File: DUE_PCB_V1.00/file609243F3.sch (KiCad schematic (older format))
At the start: 20 parts, among them J26 Motor Left, J27 Cutter Motor, J28 Motor Right, U1 MC33926, U2 MC33926

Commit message: Remove 2x4 Motor Pin Connectors
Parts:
- removed J26: Motor Left, Connector_PinSocket_2.54mm:PinSocket_2x04_P2.54mm_Vertical, symbol Connector_Generic:Conn_02x04_Top_Bottom
- removed J27: Cutter Motor, Connector_PinSocket_2.54mm:PinSocket_2x04_P2.54mm_Vertical, symbol Connector_Generic:Conn_02x04_Top_Bottom
- removed J28: Motor Right, Connector_PinSocket_2.54mm:PinSocket_2x04_P2.54mm_Vertical, symbol Connector_Generic:Conn_02x04_Top_Bottom
- removed JP4, JP5, JP6: 5V, Connector_PinSocket_2.54mm:PinSocket_1x02_P2.54mm_Vertical, symbol Jumper:Jumper_2_Open
- removed R17, R19, R21, R23, R25, R27: 1.5KO, Resistor_THT:R_Axial_DIN0207_L6.3mm_D2.5mm_P2.54mm_Vertical, symbol Device:R
- removed R18, R20, R22, R24, R26, R28: 1KO, Resistor_THT:R_Axial_DIN0207_L6.3mm_D2.5mm_P2.54mm_Vertical, symbol Device:R
- added D5: 1N5819, Diode_THT:D_DO-41_SOD81_P10.16mm_Horizontal, symbol Diode:1N5819
- added J32: 24V In, TerminalBlock:TerminalBlock_bornier-2_P5.08mm, symbol Connector:Screw_Terminal_01x02
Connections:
- net +24V: now also D5.1 (K)
- net GND: now also J32.1 (Pin_1)
- new net: D5.2 (A), J32.2 (Pin_2)
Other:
- moved on the sheet: U1, U2

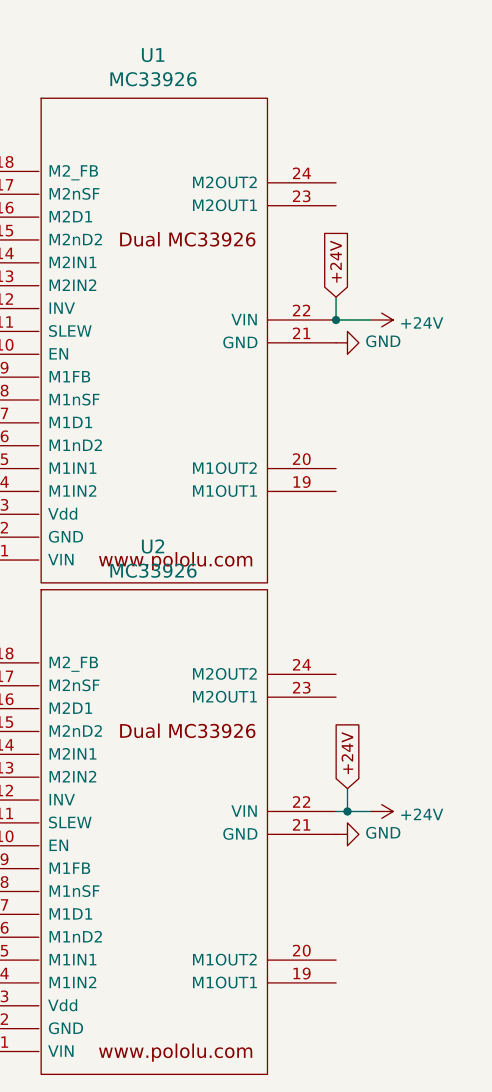
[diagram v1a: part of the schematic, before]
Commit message: Add Connector 24V for Motor & Cutter
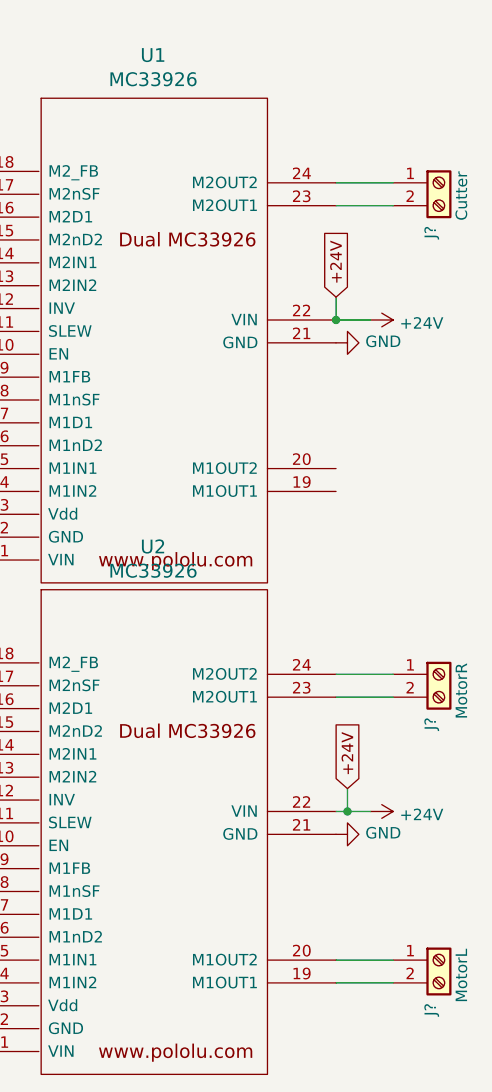
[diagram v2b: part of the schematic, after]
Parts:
- added J?: Cutter, TerminalBlock:TerminalBlock_bornier-2_P5.08mm, symbol Connector:Screw_Terminal_01x02
- added J?: MotorR, TerminalBlock:TerminalBlock_bornier-2_P5.08mm, symbol Connector:Screw_Terminal_01x02
- added J?: MotorL, TerminalBlock:TerminalBlock_bornier-2_P5.08mm, symbol Connector:Screw_Terminal_01x02
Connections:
- net at U2.19 (M1OUT1): now also J?.2 (Pin_2)
- net at U2.20 (M1OUT2): now also J?.1 (Pin_1)
- net at U2.23 (M2OUT1): now also J?.2 (Pin_2)
- net at U2.24 (M2OUT2): now also J?.1 (Pin_1)
- net at U1.23 (M2OUT1): now also J?.2 (Pin_2)
- net at U1.24 (M2OUT2): now also J?.1 (Pin_1)
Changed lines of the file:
@@
 Wire Wire Line
 	1350 950  1500 950
+$Comp
+L Connector:Screw_Terminal_01x02 J?
+U 1 1 60E7534A
+P 6350 1350
+F 0 "J?" V 6314 1162 50  0000 R CNN
+F 1 "Cutter" V 6450 1400 50  0000 R CNN
+F 2 "TerminalBlock:TerminalBlock_bornier-2_P5.08mm" H 6350 1350 50  0001 C CNN
+F 3 "~" H 6350 1350 50  0001 C CNN
+	1    6350 1350
+	1    0    0    -1
+$EndComp
+Wire Wire Line
+	5900 1350 6150 1350
+Wire Wire Line
+	5900 1450 6150 1450
+$Comp
+L Connector:Screw_Terminal_01x02 J?
+U 1 1 60E78788
+P 6350 3500
+F 0 "J?" V 6314 3312 50  0000 R CNN
+F 1 "MotorR" V 6450 3550 50  0000 R CNN
+F 2 "TerminalBlock:TerminalBlock_bornier-2_P5.08mm" H 6350 3500 50  0001 C CNN
+F 3 "~" H 6350 3500 50  0001 C CNN
+	1    6350 3500
+	1    0    0    -1
+$EndComp
+Wire Wire Line
+	5900 3500 6150 3500
+Wire Wire Line
+	5900 3600 6150 3600
+$Comp
+L Connector:Screw_Terminal_01x02 J?
+U 1 1 60E799F8
+P 6350 4750
+F 0 "J?" V 6314 4562 50  0000 R CNN
+F 1 "MotorL" V 6450 4800 50  0000 R CNN
+F 2 "TerminalBlock:TerminalBlock_bornier-2_P5.08mm" H 6350 4750 50  0001 C CNN
+F 3 "~" H 6350 4750 50  0001 C CNN
+	1    6350 4750
+	1    0    0    -1
+$EndComp
+Wire Wire Line
+	5900 4750 6150 4750
+Wire Wire Line
+	5900 4850 6150 4850
 $EndSCHEMATC

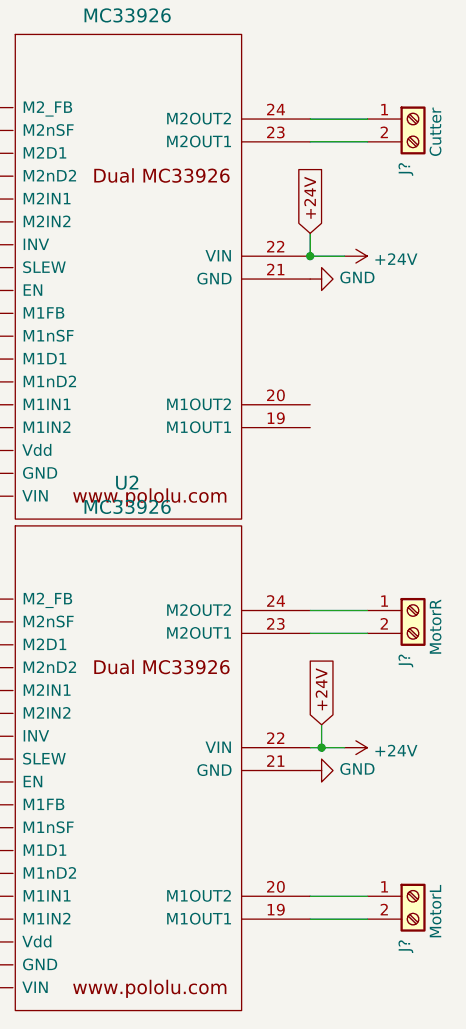
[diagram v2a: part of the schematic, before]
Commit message: Add Pin Description on PCB
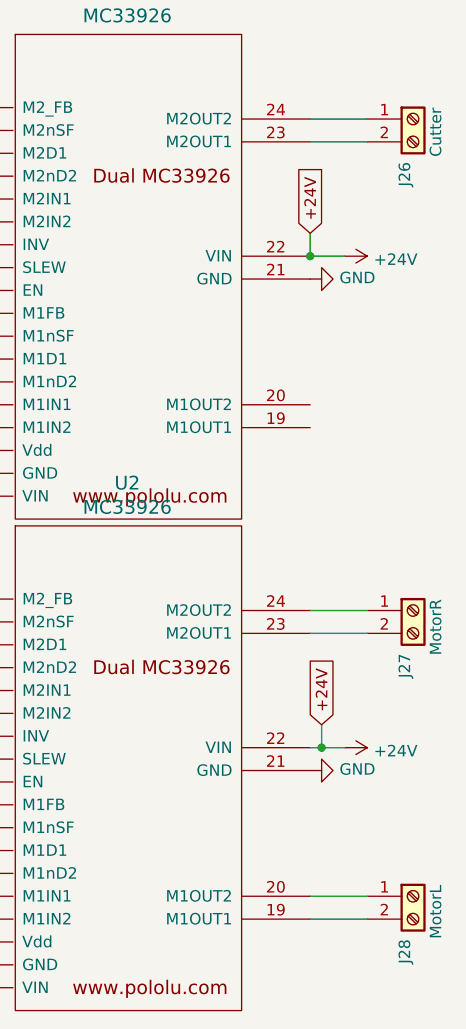
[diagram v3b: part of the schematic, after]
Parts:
- gave numbers to parts that had none: 3
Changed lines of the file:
@@
 	1350 950  1500 950
 $Comp
-L Connector:Screw_Terminal_01x02 J?
+L Connector:Screw_Terminal_01x02 J26
 U 1 1 60E7534A
 P 6350 1350
-F 0 "J?" V 6314 1162 50  0000 R CNN
+F 0 "J26" V 6314 1162 50  0000 R CNN
 F 1 "Cutter" V 6450 1400 50  0000 R CNN
 F 2 "TerminalBlock:TerminalBlock_bornier-2_P5.08mm" H 6350 1350 50  0001 C CNN
@@
 	5900 1450 6150 1450
 $Comp
-L Connector:Screw_Terminal_01x02 J?
+L Connector:Screw_Terminal_01x02 J27
 U 1 1 60E78788
 P 6350 3500
-F 0 "J?" V 6314 3312 50  0000 R CNN
+F 0 "J27" V 6314 3312 50  0000 R CNN
 F 1 "MotorR" V 6450 3550 50  0000 R CNN
 F 2 "TerminalBlock:TerminalBlock_bornier-2_P5.08mm" H 6350 3500 50  0001 C CNN
@@
 	5900 3600 6150 3600
 $Comp
-L Connector:Screw_Terminal_01x02 J?
+L Connector:Screw_Terminal_01x02 J28
 U 1 1 60E799F8
 P 6350 4750
-F 0 "J?" V 6314 4562 50  0000 R CNN
+F 0 "J28" V 6314 4562 50  0000 R CNN
 F 1 "MotorL" V 6450 4800 50  0000 R CNN
 F 2 "TerminalBlock:TerminalBlock_bornier-2_P5.08mm" H 6350 4750 50  0001 C CNN

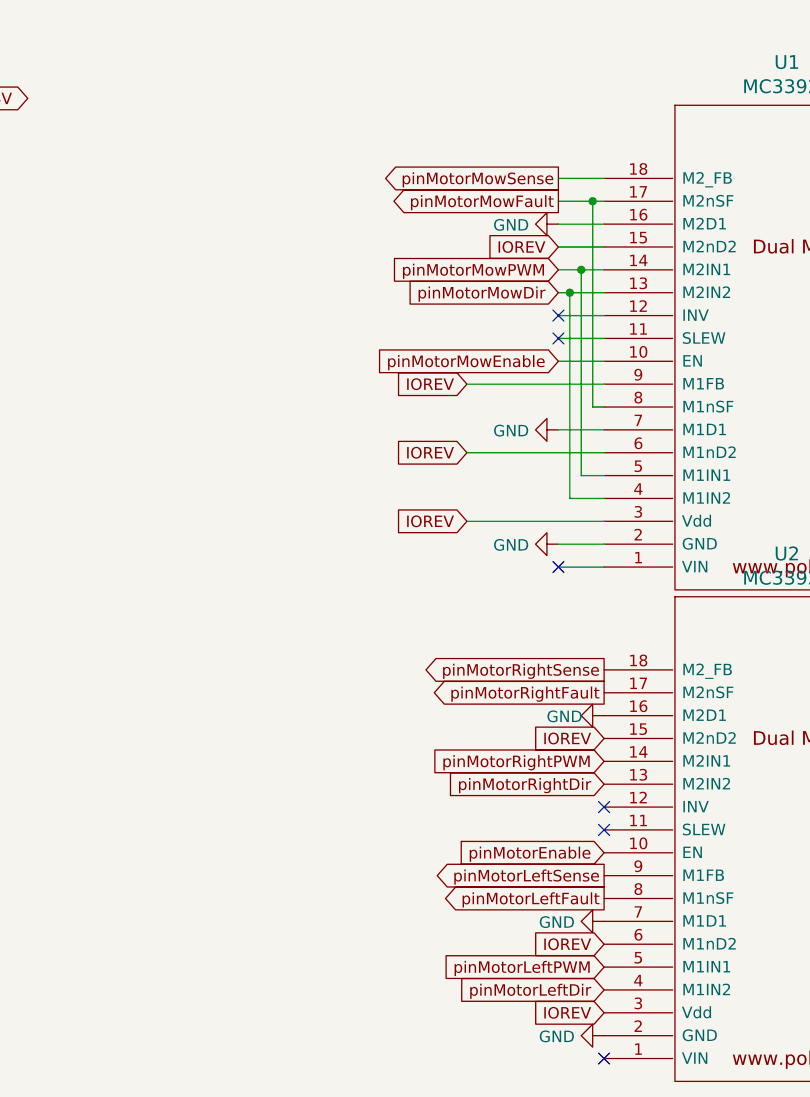
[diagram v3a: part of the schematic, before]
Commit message: Add Zener Diode
3.3 V zener diode to clamp the current sense output voltage to a maximum of ~3.3 V
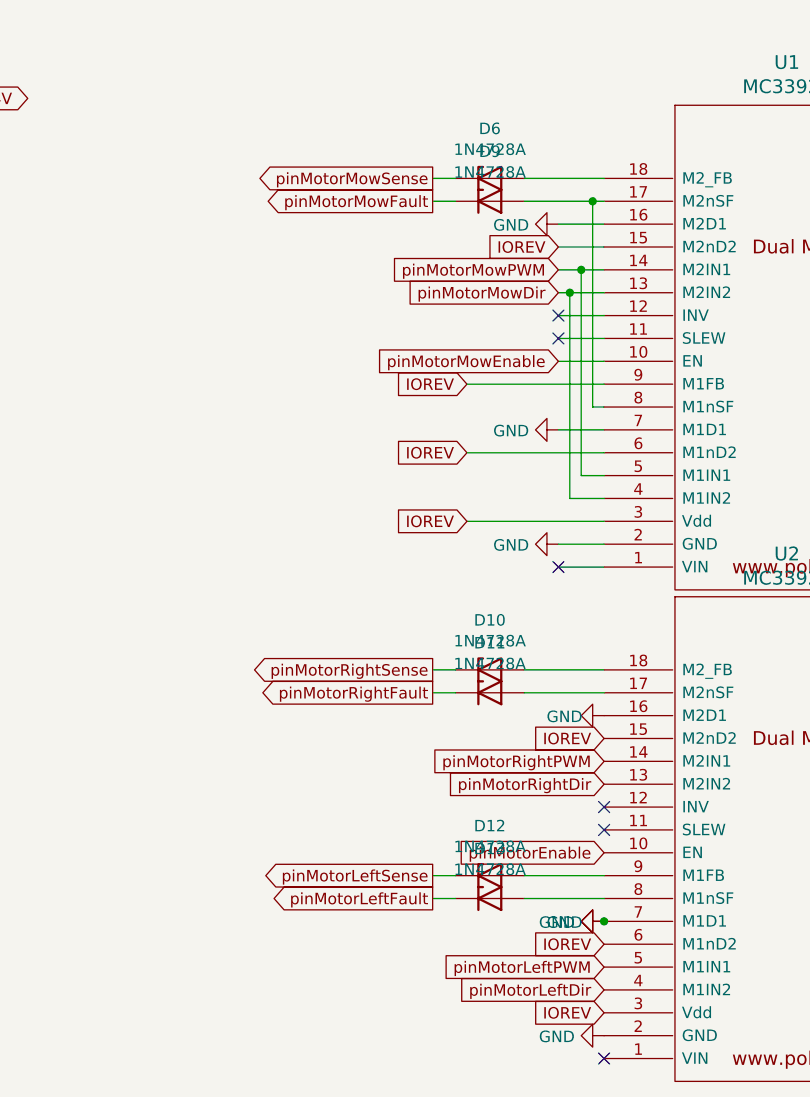
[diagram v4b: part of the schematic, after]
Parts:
- added D10, D11, D12, D13, D6, D9: 1N4728A, Diode_THT:D_DO-41_SOD81_P10.16mm_Horizontal, symbol Diode:1N47xxA
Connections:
- net pinMotorLeftFault: now also D13.1 (K); no longer U2.8 (M1nSF)
- net pinMotorLeftSense: now also D12.1 (K); no longer U2.9 (M1FB)
- net pinMotorMowFault: now also D9.1 (K); no longer U1.17 (M2nSF), U1.8 (M1nSF)
- net pinMotorMowSense: now also D6.1 (K); no longer U1.18 (M2_FB)
- net pinMotorRightFault: now also D11.1 (K); no longer U2.17 (M2nSF)
- net pinMotorRightSense: now also D10.1 (K); no longer U2.18 (M2_FB)
- new net: D11.2 (A), U2.17 (M2nSF)
- new net: D10.2 (A), U2.18 (M2_FB)
- new net: D13.2 (A), U2.8 (M1nSF)
- new net: D12.2 (A), U2.9 (M1FB)
- new net: D9.2 (A), U1.17 (M2nSF), U1.8 (M1nSF)
- new net: D6.2 (A), U1.18 (M2_FB)
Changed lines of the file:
@@
 Text GLabel 4300 4250 0    50   Input ~ 0
 pinMotorEnable
-Text GLabel 4300 3450 0    50   Output ~ 0
+Text GLabel 3550 3450 0    50   Output ~ 0
 pinMotorRightSense
-Text GLabel 4300 3550 0    50   Output ~ 0
+Text GLabel 3550 3550 0    50   Output ~ 0
 pinMotorRightFault
 $Comp
@@
 NoConn ~ 4300 4050
 NoConn ~ 4300 4150
-Text GLabel 4300 4350 0    50   Output ~ 0
+Text GLabel 3550 4350 0    50   Output ~ 0
 pinMotorLeftSense
-Text GLabel 4300 4450 0    50   Output ~ 0
+Text GLabel 3550 4450 0    50   Output ~ 0
 pinMotorLeftFault
 $Comp
@@
 	0    1    1    0
 $EndComp
-Text GLabel 4100 1300 0    50   Output ~ 0
+Text GLabel 3550 1300 0    50   Output ~ 0
 pinMotorMowSense
-Text GLabel 4100 1400 0    50   Output ~ 0
+Text GLabel 3550 1400 0    50   Output ~ 0
 pinMotorMowFault
 Text GLabel 4100 1600 0    50   Input ~ 0
@@
 pinMotorMowEnable
 Wire Wire Line
-	4100 1300 4300 1300
-Wire Wire Line
 	4100 1500 4300 1500
 Wire Wire Line
@@
 Wire Wire Line
 	4100 3000 4300 3000
-Wire Wire Line
-	4100 1400 4250 1400
 Wire Wire Line
 	4300 2300 4250 2300
@@
 Wire Wire Line
 	5900 4850 6150 4850
+$Comp
+L Diode:1N47xxA D6
+U 1 1 609D8865
+P 3800 1300
+F 0 "D6" H 3800 1517 50  0000 C CNN
+F 1 "1N4728A" H 3800 1426 50  0000 C CNN
+F 2 "Diode_THT:D_DO-41_SOD81_P10.16mm_Horizontal" H 3800 1125 50  0001 C CNN
+F 3 "https://www.vishay.com/docs/85816/1n4728a.pdf" H 3800 1300 50  0001 C CNN
+	1    3800 1300
+	1    0    0    -1
+$EndComp
+$Comp
+L Diode:1N47xxA D9
+U 1 1 609DAEC2
+P 3800 1400
+F 0 "D9" H 3800 1617 50  0000 C CNN
+F 1 "1N4728A" H 3800 1526 50  0000 C CNN
+F 2 "Diode_THT:D_DO-41_SOD81_P10.16mm_Horizontal" H 3800 1225 50  0001 C CNN
+F 3 "https://www.vishay.com/docs/85816/1n4728a.pdf" H 3800 1400 50  0001 C CNN
+	1    3800 1400
+	1    0    0    -1
+$EndComp
+Wire Wire Line
+	3950 1300 4300 1300
+Wire Wire Line
+	3550 1400 3650 1400
+Wire Wire Line
+	3950 1400 4250 1400
+Wire Wire Line
+	3550 1300 3650 1300
+$Comp
+L Diode:1N47xxA D10
+U 1 1 609E18E1
+P 3800 3450
+F 0 "D10" H 3800 3667 50  0000 C CNN
+F 1 "1N4728A" H 3800 3576 50  0000 C CNN
+F 2 "Diode_THT:D_DO-41_SOD81_P10.16mm_Horizontal" H 3800 3275 50  0001 C CNN
+F 3 "https://www.vishay.com/docs/85816/1n4728a.pdf" H 3800 3450 50  0001 C CNN
+	1    3800 3450
+	1    0    0    -1
+$EndComp
+$Comp
+L Diode:1N47xxA D11
+U 1 1 609E1AC5
+P 3800 3550
+F 0 "D11" H 3800 3767 50  0000 C CNN
+F 1 "1N4728A" H 3800 3676 50  0000 C CNN
+F 2 "Diode_THT:D_DO-41_SOD81_P10.16mm_Horizontal" H 3800 3375 50  0001 C CNN
+F 3 "https://www.vishay.com/docs/85816/1n4728a.pdf" H 3800 3550 50  0001 C CNN
+	1    3800 3550
+	1    0    0    -1
+$EndComp
+Wire Wire Line
+	3950 3450 4300 3450
+Wire Wire Line
+	3550 3550 3650 3550
+Wire Wire Line
+	3550 3450 3650 3450
+Wire Wire Line
+	3950 3550 4300 3550
+$Comp
+L power:GND #PWR?
+U 1 1 609E6ACA
+P 4300 4550
+AR Path="/609E6ACA" Ref="#PWR?"  Part="1"
+AR Path="/609243F4/609E6ACA" Ref="#PWR066"  Part="1"
+F 0 "#PWR066" H 4300 4300 50  0001 C CNN
+F 1 "GND" V 4305 4377 50  0000 C CNN
+F 2 "" H 4300 4550 50  0001 C CNN
+F 3 "" H 4300 4550 50  0001 C CNN
+	1    4300 4550
+	0    1    1    0
+$EndComp
+$Comp
+L Diode:1N47xxA D12
+U 1 1 609E6CD2
+P 3800 4350
+F 0 "D12" H 3800 4567 50  0000 C CNN
+F 1 "1N4728A" H 3800 4476 50  0000 C CNN
+F 2 "Diode_THT:D_DO-41_SOD81_P10.16mm_Horizontal" H 3800 4175 50  0001 C CNN
+F 3 "https://www.vishay.com/docs/85816/1n4728a.pdf" H 3800 4350 50  0001 C CNN
+	1    3800 4350
+	1    0    0    -1
+$EndComp
+$Comp
+L Diode:1N47xxA D13
+U 1 1 609E6CDC
+P 3800 4450
+F 0 "D13" H 3800 4667 50  0000 C CNN
+F 1 "1N4728A" H 3800 4576 50  0000 C CNN
+F 2 "Diode_THT:D_DO-41_SOD81_P10.16mm_Horizontal" H 3800 4275 50  0001 C CNN
+F 3 "https://www.vishay.com/docs/85816/1n4728a.pdf" H 3800 4450 50  0001 C CNN
+	1    3800 4450
+	1    0    0    -1
+$EndComp
+Wire Wire Line
+	3950 4350 4300 4350
+Wire Wire Line
+	3550 4450 3650 4450
+Wire Wire Line
+	3550 4350 3650 4350
+Wire Wire Line
+	3950 4450 4300 4450
+Connection ~ 4300 4550
 $EndSCHEMATC
